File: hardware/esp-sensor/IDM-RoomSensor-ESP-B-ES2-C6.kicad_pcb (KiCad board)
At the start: 4 copper layers, 110 x 70 mm, 71 parts, among them J1 IDM 43/42/41/40, J2 RS485 A/B/COM/SH, J3 USB-C, J4 EXPANSION, SW1 RESET, SW2 BOOT, U1 LMR36510ADDAR, U2 AP2112K-3.3, U3 ESP32-C6-WROOM-1-N16, U4 SHT45, U5 MCP4725A0T, U6 OPA197IDBVR, U7 ADM2587EBRWZ

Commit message: fix(hardware): use neutral B-ES2-C6 silkscreen branding
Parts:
- J1: value IDM 43/42/41/40 -> 43/42/41/40
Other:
- board text added: "43 TEMP | 42 +24V | 41 GND | 40 RH"
- board text added: "SMART CLIMATE SENSOR"
- board text added: "by Xerolux | xerolux.de | REV B-ES2-C6 | 2026"
- board text removed: "IDM ROOM SENSOR B-ES2-C6"
- board text removed: "IDM: 43 TEMP | 42 +24V | 41 GND | 40 RH"
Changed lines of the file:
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@@
 			)
 		)
-		(property "Value" "IDM 43/42/41/40"
+		(property "Value" "43/42/41/40"
 			(at 5.25 5.62 90)
 			(layer "F.Fab")
@@
 		(layer "Edge.Cuts")
 	)
-	(gr_text "IDM: 43 TEMP | 42 +24V | 41 GND | 40 RH"
-		(at 39 78 0)
+	(gr_text "43 TEMP | 42 +24V | 41 GND | 40 RH"
+		(at 37 78 0)
 		(layer "F.SilkS")
 		(effects
@@
 		)
 	)
+	(gr_text "by Xerolux | xerolux.de | REV B-ES2-C6 | 2026"
+		(at 83 14.5 0)
+		(layer "F.SilkS")
+		(effects
+			(font
+				(size 0.65 0.65)
+				(thickness 0.12)
+			)
+		)
+	)
 	(gr_text "RS485 ISOLATED"
 		(at 105 77 0)
@@
 		)
 	)
-	(gr_text "IDM ROOM SENSOR B-ES2-C6"
+	(gr_text "SMART CLIMATE SENSOR"
 		(at 83 12 0)
 		(layer "F.SilkS")

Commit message: fix(hardware): correct C6 JLCPCB part mappings
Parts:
- R9: value 21k 0.1% -> 21k 1% CAL
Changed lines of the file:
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@@
 			)
 		)
-		(property "Value" "21k 0.1%"
+		(property "Value" "21k 1% CAL"
 			(at 0 1.43 0)
 			(layer "F.Fab")

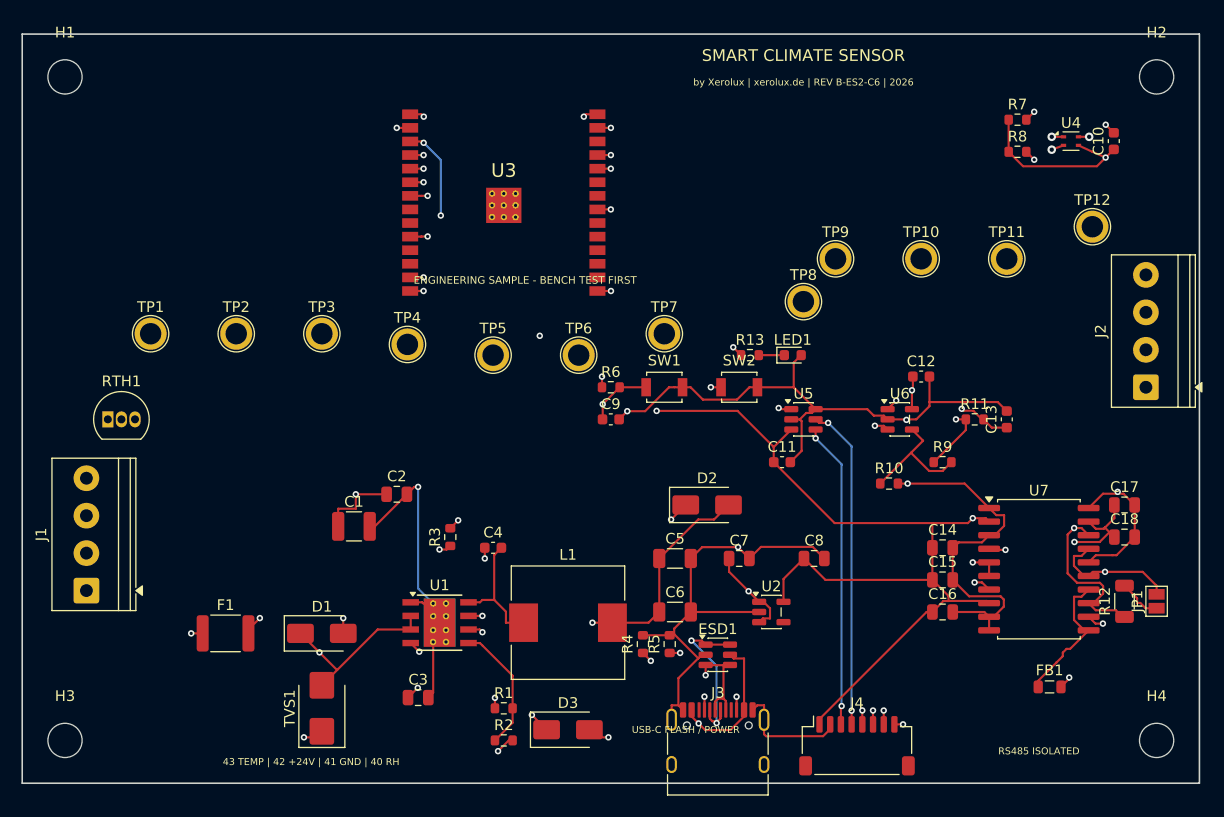
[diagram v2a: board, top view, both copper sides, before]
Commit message: fix(hardware): reduce isolated RS485 assembly cost
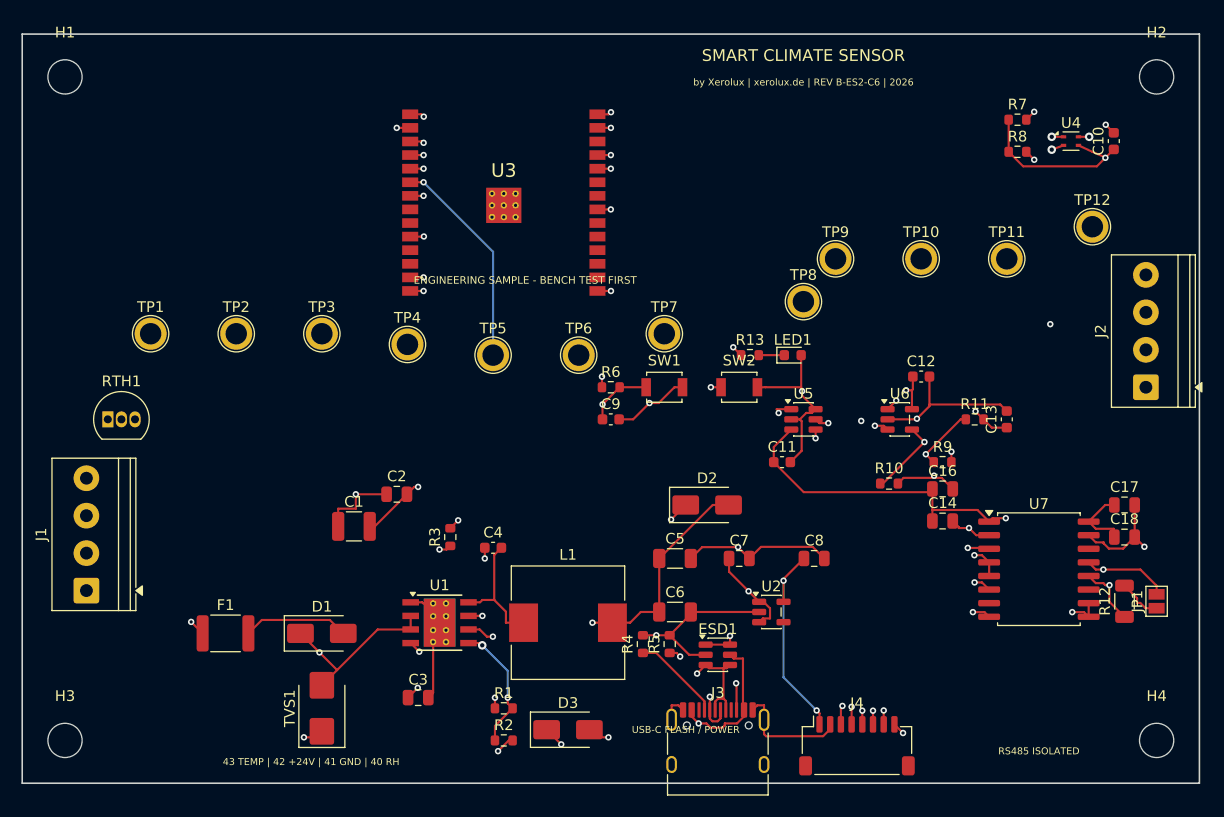
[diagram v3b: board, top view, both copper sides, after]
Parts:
- removed C15: 10n, C_0805_2012Metric
- removed FB1: 600R, L_0805_2012Metric
- U7: value ADM2587EBRWZ -> CA-IS3092W; footprint SOIC-20W_7.5x12.8mm_P1.27mm -> SOIC-16W_7.5x10.3mm_P1.27mm
- moved C16 11.5 mm to (96.0, 52.5)
- moved C14 2.50 mm to (96.0, 55.5)
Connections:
- U7 pad 1: GND -> +3V3
- U7 pad 10: GND -> RS485_COM
- U7 pad 11: ISO_GND_PWR -> (no net)
- U7 pad 12: VISO -> RS485_A
- U7 pad 13: RS485_A -> RS485_B
- U7 pad 14: ISO_GND_PWR -> (no net)
- U7 pad 15: RS485_B -> RS485_COM
- U7 pad 16: RS485_COM -> VISO
- U7 pad 2: +3V3 -> GND
- U7 pad 3: GND -> RS485_RX
- U7 pad 4: RS485_RX -> RS485_DE
- U7 pad 6: RS485_DE -> RS485_TX
- U7 pad 7: RS485_TX -> (no net)
- U7 pad 8: +3V3 -> GND
- U7 pad 9: GND -> RS485_COM
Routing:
- net GND: track 447.3 -> 119.0 mm, vias 11 -> 15
- net RS485_COM: track 68.7 -> 21.7 mm, vias 2 -> 3
- net I2C_SDA: track 126.2 -> 146.9 mm
- net VISO: track 19.5 -> 6.46 mm, vias 2 -> 0
- net ISO_GND_PWR: track 12.9 -> 0.00 mm
- net SYS_5V: track 116.0 -> 126.2 mm
- net I2C_SCL: track 124.7 -> 116.8 mm, vias 5 -> 6
- net RS485_RX: track 60.4 -> 52.5 mm
- net RS485_A: track 66.1 -> 59.7 mm
- net RS485_B: track 60.3 -> 54.8 mm
- net +3V3: track 191.0 -> 196.6 mm, vias 5 -> 6
- net 5V_BUCK: track 49.2 -> 52.6 mm
- net RS485_DE: track 61.0 -> 58.2 mm
- net VCC_BYP: track 10.9 -> 12.8 mm
- net ONEWIRE: track 59.1 -> 60.7 mm
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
